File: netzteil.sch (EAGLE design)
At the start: 43 parts

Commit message: version3
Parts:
- C10, C14, C15, C9: device resistor:C-EUC0603K -> resistor:C-EUC0805K
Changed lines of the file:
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@@
 <grid distance="0.1" unitdist="inch" unit="inch" style="lines" multiple="1" display="no" altdistance="0.01" altunitdist="inch" altunit="inch"/>
 <layers>
-<layer number="1" name="Top" color="4" fill="1" visible="no" active="no"/>
-<layer number="16" name="Bottom" color="1" fill="1" visible="no" active="no"/>
-<layer number="17" name="Pads" color="2" fill="1" visible="no" active="no"/>
-<layer number="18" name="Vias" color="2" fill="1" visible="no" active="no"/>
-<layer number="19" name="Unrouted" color="6" fill="1" visible="no" active="no"/>
-<layer number="20" name="Dimension" color="15" fill="1" visible="no" active="no"/>
-<layer number="21" name="tPlace" color="7" fill="1" visible="no" active="no"/>
-<layer number="22" name="bPlace" color="7" fill="1" visible="no" active="no"/>
-<layer number="23" name="tOrigins" color="15" fill="1" visible="no" active="no"/>
-<layer number="24" name="bOrigins" color="15" fill="1" visible="no" active="no"/>
-<layer number="25" name="tNames" color="7" fill="1" visible="no" active="no"/>
-<layer number="26" name="bNames" color="7" fill="1" visible="no" active="no"/>
-<layer number="27" name="tValues" color="7" fill="1" visible="no" active="no"/>
-<layer number="28" name="bValues" color="7" fill="1" visible="no" active="no"/>
+<layer number="1" name="Top" color="4" fill="1" visible="yes" active="no"/>
+<layer number="16" name="Bottom" color="1" fill="1" visible="yes" active="no"/>
+<layer number="17" name="Pads" color="2" fill="1" visible="yes" active="no"/>
+<layer number="18" name="Vias" color="2" fill="1" visible="yes" active="no"/>
+<layer number="19" name="Unrouted" color="6" fill="1" visible="yes" active="no"/>
+<layer number="20" name="Dimension" color="15" fill="1" visible="yes" active="no"/>
+<layer number="21" name="tPlace" color="7" fill="1" visible="yes" active="no"/>
+<layer number="22" name="bPlace" color="7" fill="1" visible="yes" active="no"/>
+<layer number="23" name="tOrigins" color="15" fill="1" visible="yes" active="no"/>
+<layer number="24" name="bOrigins" color="15" fill="1" visible="yes" active="no"/>
+<layer number="25" name="tNames" color="7" fill="1" visible="yes" active="no"/>
+<layer number="26" name="bNames" color="7" fill="1" visible="yes" active="no"/>
+<layer number="27" name="tValues" color="7" fill="1" visible="yes" active="no"/>
+<layer number="28" name="bValues" color="7" fill="1" visible="yes" active="no"/>
 <layer number="29" name="tStop" color="7" fill="3" visible="no" active="no"/>
 <layer number="30" name="bStop" color="7" fill="6" visible="no" active="no"/>
@@
 <layer number="35" name="tGlue" color="7" fill="4" visible="no" active="no"/>
 <layer number="36" name="bGlue" color="7" fill="5" visible="no" active="no"/>
-<layer number="37" name="tTest" color="7" fill="1" visible="no" active="no"/>
-<layer number="38" name="bTest" color="7" fill="1" visible="no" active="no"/>
+<layer number="37" name="tTest" color="7" fill="1" visible="yes" active="no"/>
+<layer number="38" name="bTest" color="7" fill="1" visible="yes" active="no"/>
 <layer number="39" name="tKeepout" color="4" fill="11" visible="no" active="no"/>
 <layer number="40" name="bKeepout" color="1" fill="11" visible="no" active="no"/>
@@
 <layer number="44" name="Drills" color="7" fill="1" visible="no" active="no"/>
 <layer number="45" name="Holes" color="7" fill="1" visible="no" active="no"/>
-<layer number="46" name="Milling" color="3" fill="1" visible="no" active="no"/>
-<layer number="47" name="Measures" color="7" fill="1" visible="no" active="no"/>
-<layer number="48" name="Document" color="7" fill="1" visible="no" active="no"/>
-<layer number="49" name="Reference" color="7" fill="1" visible="no" active="no"/>
-<layer number="51" name="tDocu" color="7" fill="1" visible="no" active="no"/>
-<layer number="52" name="bDocu" color="7" fill="1" visible="no" active="no"/>
+<layer number="46" name="Milling" color="3" fill="1" visible="yes" active="no"/>
+<layer number="47" name="Measures" color="7" fill="1" visible="yes" active="no"/>
+<layer number="48" name="Document" color="7" fill="1" visible="yes" active="no"/>
+<layer number="49" name="Reference" color="7" fill="1" visible="yes" active="no"/>
+<layer number="51" name="tDocu" color="7" fill="1" visible="yes" active="no"/>
+<layer number="52" name="bDocu" color="7" fill="1" visible="yes" active="no"/>
 <layer number="91" name="Nets" color="2" fill="1" visible="yes" active="yes"/>
 <layer number="92" name="Busses" color="1" fill="1" visible="yes" active="yes"/>
@@
 <part name="GND4" library="supply1" deviceset="GND" device=""/>
 <part name="C8" library="resistor" deviceset="C-EU" device="C0603K" value="1µ"/>
-<part name="C9" library="resistor" deviceset="C-EU" device="C0603K" value="470n"/>
-<part name="C10" library="resistor" deviceset="C-EU" device="C0603K" value="4µ7"/>
+<part name="C9" library="resistor" deviceset="C-EU" device="C0805K" value="470n"/>
+<part name="C10" library="resistor" deviceset="C-EU" device="C0805K" value="4µ7"/>
 <part name="C11" library="resistor" deviceset="C-EU" device="C0603K" value="100n"/>
 <part name="C12" library="resistor" deviceset="C-EU" device="C0603K" value="33n"/>
@@
 <part name="GND13" library="supply1" deviceset="GND" device=""/>
 <part name="P+4" library="supply1" deviceset="+5V" device=""/>
-<part name="C14" library="resistor" deviceset="C-EU" device="C0603K" value="100n"/>
-<part name="C15" library="resistor" deviceset="C-EU" device="C0603K" value="100n"/>
+<part name="C14" library="resistor" deviceset="C-EU" device="C0805K" value="100n"/>
+<part name="C15" library="resistor" deviceset="C-EU" device="C0805K" value="100n"/>
 <part name="P+5" library="supply1" deviceset="+5V" device=""/>
 <part name="P+6" library="supply1" deviceset="+5V" device=""/>

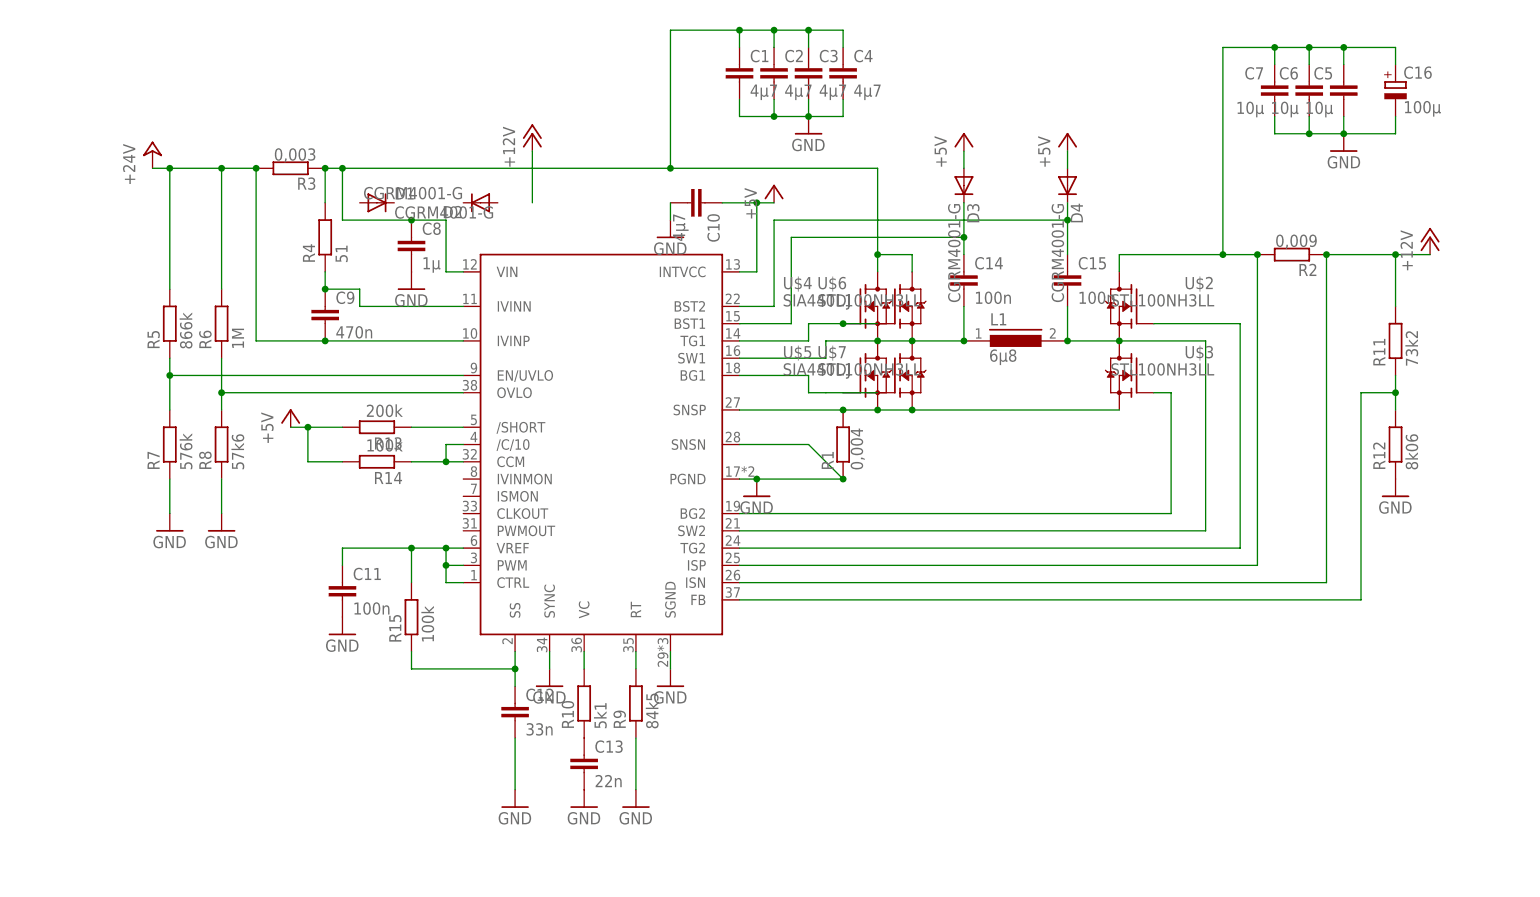
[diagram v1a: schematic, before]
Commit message: an platinenbelichter gesendet, hohlstecker verpolt
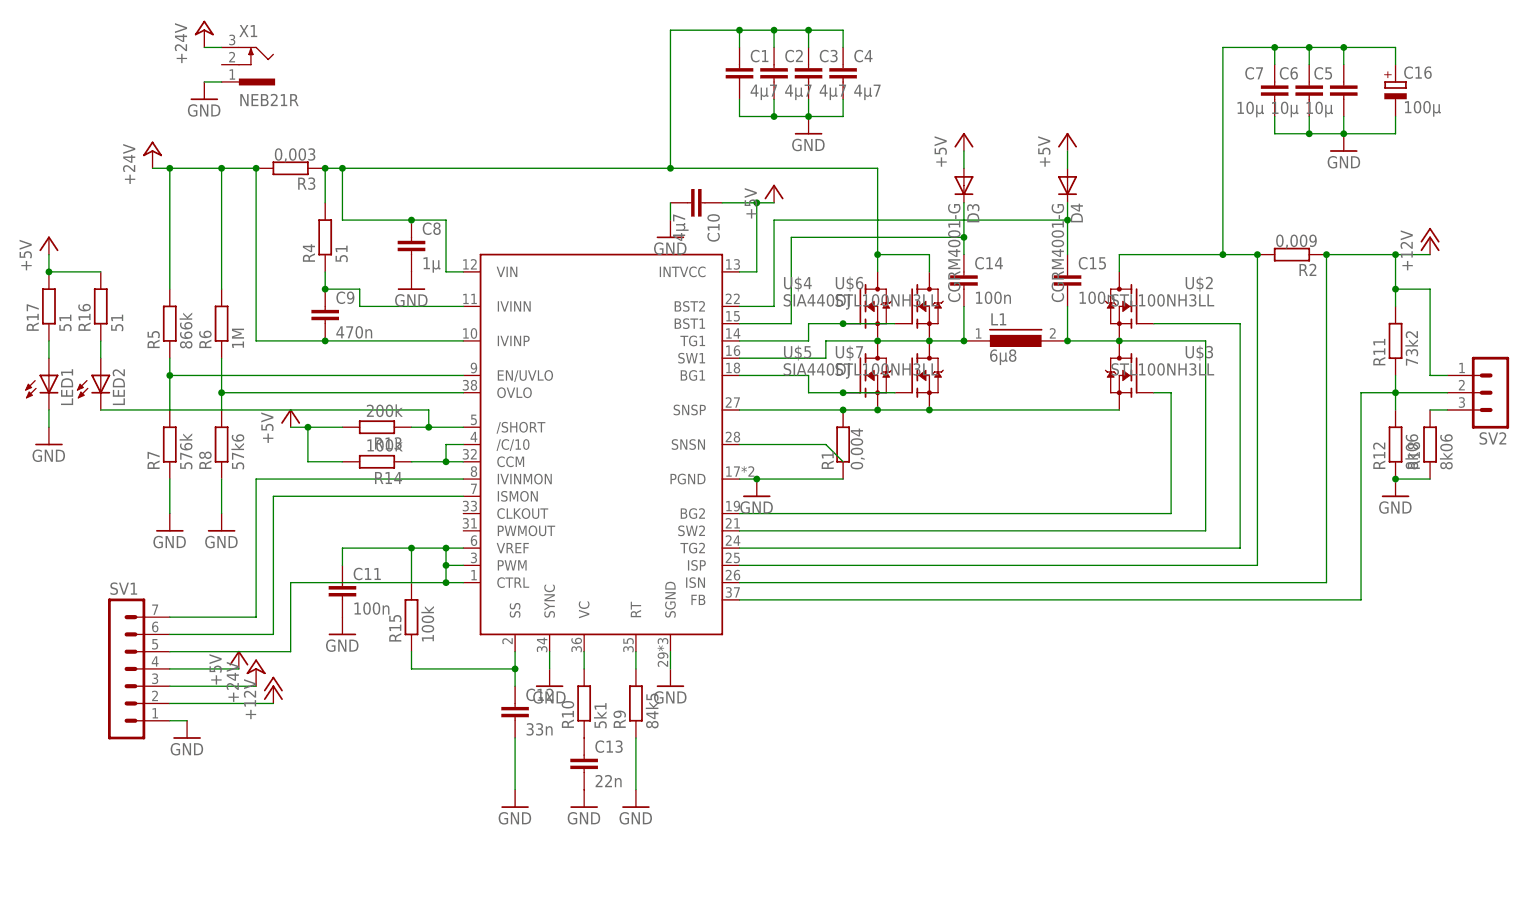
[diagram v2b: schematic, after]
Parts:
- removed D1, D2: CGRM4001-G, diode:CGRM4001-G
- added LED1, LED2: (no value), led:LEDSML0805
- added R16, R17: 51, resistor:R-EU_M0805
- added R18: 8k06, resistor:R-EU_M0805
- added SV1: (no value), con-lstb:MA07-1
- added SV2: (no value), con-lstb:MA03-1
- added X1: NEB21R, con-lumberg:NEB21R
- C11, C12, C13, C8: device resistor:C-EUC0603K -> resistor:C-EUC0805K
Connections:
- net N$11 renamed BST1
- net N$3 renamed TG1
- net N$4 renamed BG1
- net N$6 renamed BG2
- net N$7 renamed BST2
- net N$8 renamed TG2
- new net N$1: U$1.SNSN
- new net N$2: SV1.6, U$1.ISMON
- new net N$3: SV1.7, U$1.IVINMON
- new net N$4: LED1.A, R17.1
- new net N$5: LED2.A, R16.1
- new net N$6: R18.2, SV2.3
- net +12V: now also SV1.2, SV2.1
- net +24V: now also SV1.3, X1.3
- net +5V: now also R16.2, R17.2, SV1.4
- net GND: now also LED1.C, R18.1, SV1.1, X1.1; no longer U$1.SNSN
- net N$17: now also SV2.2
- net N$20: now also LED2.C
- net N$25: now also SV1.5
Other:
- moved on the sheet: U$6, U$7

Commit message: platine V1 gefertigt
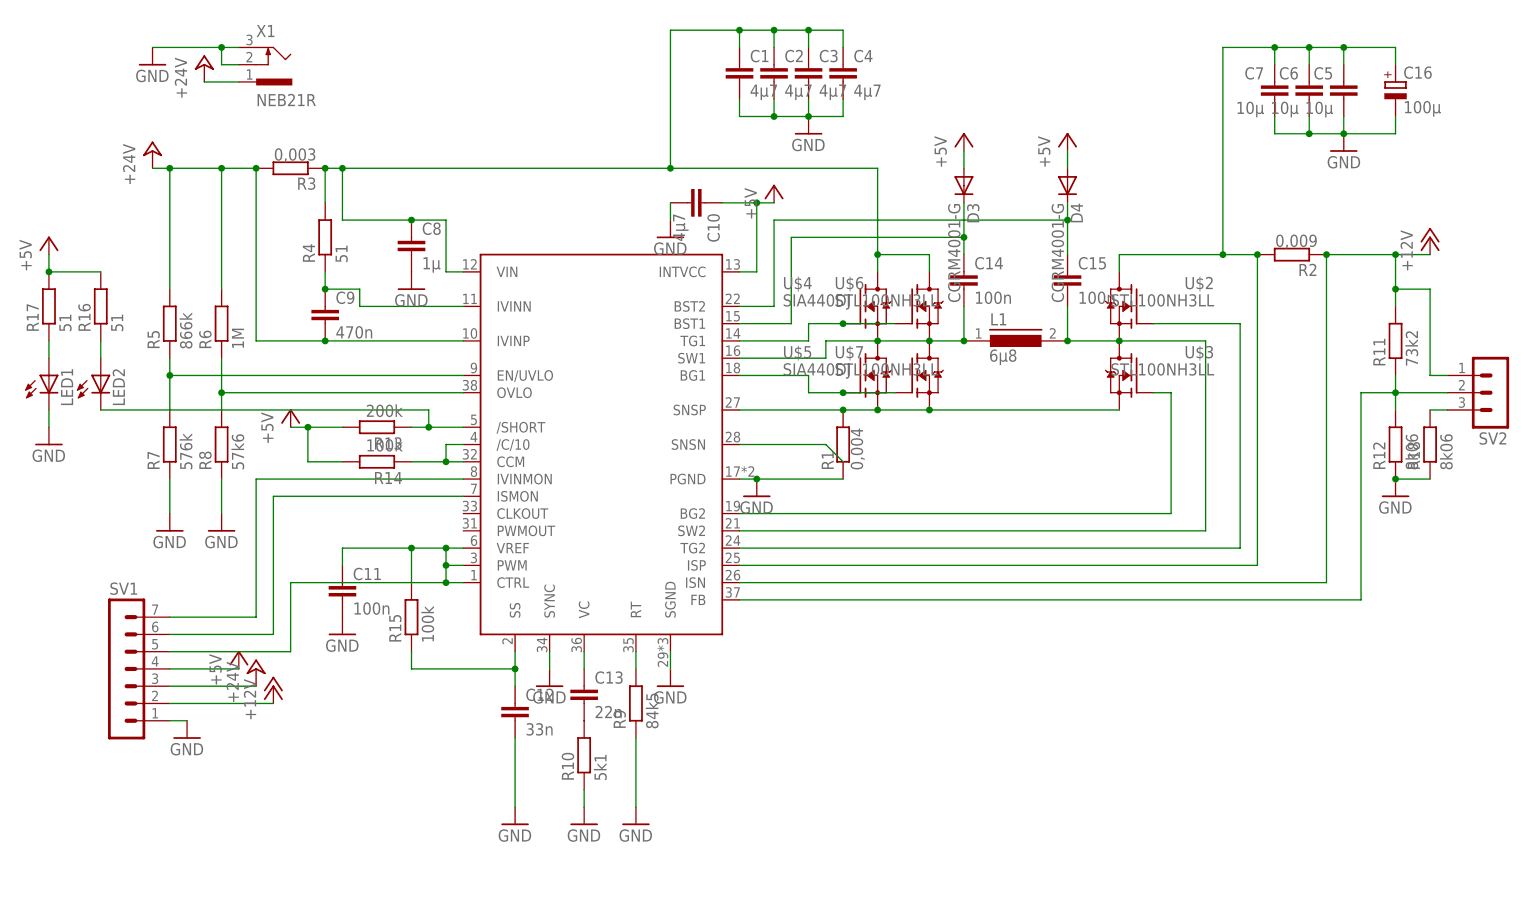
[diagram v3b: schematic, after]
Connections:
- removed net N$21: C13.1, R10.1
- removed net N$23: R10.2, U$1.VC
- new net N$7: C13.2, R10.2
- new net N$8: C13.1, U$1.VC
- net +24V: now also X1.1; no longer X1.3
- net GND: now also R10.1, X1.2, X1.3; no longer C13.2, X1.1
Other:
- moved on the sheet: C13, R10, X1
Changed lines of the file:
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@@
 <instance part="C11" gate="G$1" x="45.72" y="35.56"/>
 <instance part="C12" gate="G$1" x="71.12" y="17.78"/>
-<instance part="C13" gate="G$1" x="81.28" y="10.16"/>
+<instance part="C13" gate="G$1" x="81.28" y="20.32"/>
 <instance part="R4" gate="G$1" x="43.18" y="86.36" rot="R90"/>
 <instance part="R5" gate="G$1" x="20.32" y="73.66" rot="R90"/>
@@
 <instance part="R8" gate="G$1" x="27.94" y="55.88" rot="R90"/>
 <instance part="R9" gate="G$1" x="88.9" y="17.78" rot="R90"/>
-<instance part="R10" gate="G$1" x="81.28" y="17.78" rot="R90"/>
+<instance part="R10" gate="G$1" x="81.28" y="10.16" rot="R90"/>
 <instance part="R11" gate="G$1" x="200.66" y="71.12" rot="R90"/>
 <instance part="R12" gate="G$1" x="200.66" y="55.88" rot="R90"/>
@@
 <instance part="GND5" gate="1" x="20.32" y="43.18"/>
 <instance part="GND6" gate="1" x="27.94" y="43.18"/>
-<instance part="GND7" gate="1" x="71.12" y="2.54"/>
+<instance part="GND7" gate="1" x="71.12" y="0"/>
 <instance part="GND8" gate="1" x="76.2" y="20.32"/>
-<instance part="GND9" gate="1" x="81.28" y="2.54"/>
-<instance part="GND10" gate="1" x="88.9" y="2.54"/>
+<instance part="GND9" gate="1" x="81.28" y="0"/>
+<instance part="GND10" gate="1" x="88.9" y="0"/>
 <instance part="GND11" gate="1" x="45.72" y="27.94"/>
 <instance part="GND12" gate="1" x="55.88" y="78.74"/>
@@
 <instance part="GND16" gate="1" x="2.54" y="55.88"/>
 <instance part="P+3" gate="1" x="2.54" y="86.36"/>
-<instance part="X1" gate="G$1" x="33.02" y="111.76"/>
-<instance part="GND17" gate="1" x="25.4" y="106.68"/>
-<instance part="P+11" gate="1" x="25.4" y="116.84"/>
+<instance part="X1" gate="G$1" x="35.56" y="111.76"/>
+<instance part="GND17" gate="1" x="17.78" y="111.76"/>
+<instance part="P+11" gate="1" x="25.4" y="111.76"/>
 <instance part="R18" gate="G$1" x="205.74" y="55.88" rot="R90"/>
 </instances>
@@
 </segment>
 <segment>
-<pinref part="X1" gate="G$1" pin="3"/>
+<pinref part="X1" gate="G$1" pin="1"/>
 <pinref part="P+11" gate="1" pin="+24V"/>
-<wire x1="27.94" y1="114.3" x2="25.4" y2="114.3" width="0.1524" layer="91"/>
+<wire x1="30.48" y1="109.22" x2="25.4" y2="109.22" width="0.1524" layer="91"/>
 </segment>
 </net>
@@
 </segment>
 <segment>
-<pinref part="C13" gate="G$1" pin="2"/>
-<pinref part="GND9" gate="1" pin="GND"/>
-</segment>
-<segment>
 <pinref part="C12" gate="G$1" pin="2"/>
 <pinref part="GND7" gate="1" pin="GND"/>
-<wire x1="71.12" y1="12.7" x2="71.12" y2="5.08" width="0.1524" layer="91"/>
+<wire x1="71.12" y1="12.7" x2="71.12" y2="2.54" width="0.1524" layer="91"/>
 </segment>
 <segment>
@@
 <pinref part="R9" gate="G$1" pin="1"/>
 <pinref part="GND10" gate="1" pin="GND"/>
-<wire x1="88.9" y1="12.7" x2="88.9" y2="5.08" width="0.1524" layer="91"/>
+<wire x1="88.9" y1="12.7" x2="88.9" y2="2.54" width="0.1524" layer="91"/>
 </segment>
 <segment>
@@
 </segment>
 <segment>
-<pinref part="X1" gate="G$1" pin="1"/>
+<pinref part="X1" gate="G$1" pin="3"/>
 <pinref part="GND17" gate="1" pin="GND"/>
-<wire x1="27.94" y1="109.22" x2="25.4" y2="109.22" width="0.1524" layer="91"/>
+<wire x1="30.48" y1="114.3" x2="27.94" y2="114.3" width="0.1524" layer="91"/>
+<pinref part="X1" gate="G$1" pin="2"/>
+<wire x1="27.94" y1="114.3" x2="17.78" y2="114.3" width="0.1524" layer="91"/>
+<wire x1="30.48" y1="111.76" x2="27.94" y2="111.76" width="0.1524" layer="91"/>
+<wire x1="27.94" y1="111.76" x2="27.94" y2="114.3" width="0.1524" layer="91"/>
+<junction x="27.94" y="114.3"/>
+</segment>
+<segment>
+<pinref part="GND9" gate="1" pin="GND"/>
+<pinref part="R10" gate="G$1" pin="1"/>
+<wire x1="81.28" y1="5.08" x2="81.28" y2="2.54" width="0.1524" layer="91"/>
 </segment>
 </net>
@@
 </segment>
 </net>
-<net name="N$21" class="0">
-<segment>
-<pinref part="R10" gate="G$1" pin="1"/>
-<pinref part="C13" gate="G$1" pin="1"/>
-</segment>
-</net>
 <net name="N$22" class="0">
 <segment>
@@
 <wire x1="55.88" y1="22.86" x2="71.12" y2="22.86" width="0.1524" layer="91"/>
 <junction x="71.12" y="22.86"/>
-</segment>
-</net>
-<net name="N$23" class="0">
-<segment>
-<pinref part="U$1" gate="G$1" pin="VC"/>
-<pinref part="R10" gate="G$1" pin="2"/>
-<wire x1="81.28" y1="25.4" x2="81.28" y2="22.86" width="0.1524" layer="91"/>
 </segment>
 </net>
@@
 </segment>
 </net>
+<net name="N$7" class="0">
+<segment>
+<pinref part="R10" gate="G$1" pin="2"/>
+<pinref part="C13" gate="G$1" pin="2"/>
+</segment>
+</net>
+<net name="N$8" class="0">
+<segment>
+<pinref part="U$1" gate="G$1" pin="VC"/>
+<pinref part="C13" gate="G$1" pin="1"/>
+<wire x1="81.28" y1="22.86" x2="81.28" y2="25.4" width="0.1524" layer="91"/>
+</segment>
+</net>
